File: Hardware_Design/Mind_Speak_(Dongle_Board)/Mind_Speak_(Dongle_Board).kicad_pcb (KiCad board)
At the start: 2 copper layers, 38 x 24.5 mm, 27 parts, among them J1 USB_A, J3 Conn_01x05_Pin, J4 Conn_01x05_Pin, SW3 SW_MEC_5E, U1 FT231XQ, U2 NINA-B30x

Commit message: Dongle Layout Finished
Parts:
- added C14: 0.1uF, PCM_SparkFun-Capacitor:C_0402_1005Metric, F.Cu at (120.3, 72.6)
- added G***: LOGO, Graphics:Mo3_Tech_Logo, F.Cu at (104.8, 57.7)
- moved C11 21.4 mm to (124.0, 72.1), turned to 180 degrees
- moved R5 13.9 mm to (108.9, 70.3)
- moved D4 12.5 mm to (108.3, 71.7), turned to 180 degrees
- moved C13 11.6 mm to (103.0, 69.3), turned to 180 degrees
- moved R6 11.6 mm to (109.9, 68.9), turned to 180 degrees
- moved SW3 11.2 mm to (112.1, 60.5), turned to -90 degrees
- moved R7 9.03 mm to (111.3, 64.0)
- moved R4 6.82 mm to (106.8, 61.3)
- moved G* 5.66 mm to (104.6, 63.0)
- moved J4 2.86 mm to (117.2, 56.2)
- moved D5 1.79 mm to (108.8, 63.5), turned to -90 degrees
- moved D3 1.53 mm to (101.7, 71.0)
- moved L1 1.47 mm to (99.2, 60.6)
- moved D2 1.34 mm to (101.3, 63.2)
- moved C2 1.28 mm to (101.0, 64.3)
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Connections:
- J3 pad 2: SWD_CLK -> SWD_IO
- J3 pad 3: SWD_IO -> SWD_CLK
- U2 pad 18: unconnected-(U2-GPIO_18-Pad18) -> Net-(J4-Pin_5)
- U2 pad 20: unconnected-(U2-GPIO_20-Pad20) -> Net-(J4-Pin_4)
- U2 pad 21: unconnected-(U2-GPIO_21-Pad21) -> Net-(J4-Pin_3)
- U2 pad 22: unconnected-(U2-GPIO_22-Pad22) -> Net-(J4-Pin_2)
- U2 pad 23: unconnected-(U2-GPIO_23-Pad23) -> Net-(J4-Pin_1)
- U2 pad 35: Net-(J4-Pin_5) -> unconnected-(U2-GPIO_35-Pad35)
- U2 pad 36: Net-(J4-Pin_4) -> unconnected-(U2-GPIO_36-Pad36)
- U2 pad 37: Net-(J4-Pin_3) -> unconnected-(U2-GPIO_37-Pad37)
- U2 pad 38: Net-(J4-Pin_2) -> unconnected-(U2-GPIO_38-Pad38)
- U2 pad 39: Net-(J4-Pin_1) -> unconnected-(U2-GPIO_39-Pad39)
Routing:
- net NINA_RST: track 0.00 -> 42.3 mm, vias 0 -> 4
- net +3V3: track 0.00 -> 28.2 mm, vias 0 -> 2
- net GND: track 0.00 -> 20.4 mm, vias 0 -> 17
- net NINA_PWR: track 0.00 -> 18.5 mm
- net SWD_IO: track 0.00 -> 14.6 mm, vias 0 -> 2
- net Net-(J1-GND): track 0.00 -> 13.7 mm
- net FTDI_RX: track 0.00 -> 12.5 mm
- net FTDI_TX: track 0.00 -> 11.8 mm, vias 0 -> 2
- net SWD_CLK: track 0.00 -> 9.29 mm, vias 0 -> 2
- net VBUS: track 0.00 -> 8.92 mm
- net Net-(J1-D+): track 0.00 -> 8.40 mm
- net Net-(U1-CBUS2): track 0.00 -> 7.97 mm
- net Net-(J1-D-): track 0.00 -> 7.83 mm
- net Net-(J4-Pin_5): track 0.00 -> 7.36 mm
- net Net-(J4-Pin_4): track 0.00 -> 7.14 mm
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- added copper zone on B.Cu, net GND
- added copper zone on F.Cu, net GND
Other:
- board text added: "BLE_PWR"
- board text added: "GND"
- board text added: "GPIO_18"
- board text added: "GPIO_20"
- board text added: "GPIO_21"
- board text added: "GPIO_22"
- board text added: "GPIO_23"
- board text added: "RESET"
- board text added: "SWD"
- board text added: "SWD_CLK"
- board text added: "SWD_IO"
- board text added: "SWD_RST"
- board text added: "SWD_VCC"
- board text added: "USB"

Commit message: Edit In Layout Of Main Board
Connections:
- J1 pad SH: unconnected-(J1-Shield-PadSH)_1 -> GND
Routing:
- net GND: track 20.4 -> 16.0 mm, vias 17 -> 26
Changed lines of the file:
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@@
 			(unit
 				(name "A")
-				(pins "1" "2" "3")
+				(pins "4" "1" "2" "3")
 			)
 		)
@@
 			(solder_mask_margin 0.102)
 		)
-		(pad "SH1" smd rect
+		(pad "4" smd rect
 			(at -3.65 -1.1)
 			(size 1 0.8)
 			(layers "F.Cu" "F.Mask" "F.Paste")
+			(net "GND")
+			(pinfunction "SHIELD_4")
+			(pintype "passive")
 			(solder_mask_margin 0.102)
 		)
-		(pad "SH2" smd rect
-			(at 3.65 -1.1)
+		(pad "4" smd rect
+			(at -3.65 1.1)
 			(size 1 0.8)
 			(layers "F.Cu" "F.Mask" "F.Paste")
+			(net "GND")
+			(pinfunction "SHIELD_4")
+			(pintype "passive")
 			(solder_mask_margin 0.102)
 		)
-		(pad "SH3" smd rect
-			(at -3.65 1.1)
+		(pad "4" smd rect
+			(at 3.65 -1.1)
 			(size 1 0.8)
 			(layers "F.Cu" "F.Mask" "F.Paste")
+			(net "GND")
+			(pinfunction "SHIELD_4")
+			(pintype "passive")
 			(solder_mask_margin 0.102)
 		)
-		(pad "SH4" smd rect
+		(pad "4" smd rect
 			(at 3.65 1.1)
 			(size 1 0.8)
 			(layers "F.Cu" "F.Mask" "F.Paste")
+			(net "GND")
+			(pinfunction "SHIELD_4")
+			(pintype "passive")
 			(solder_mask_margin 0.102)
 		)
@@
 			(layers "*.Cu" "*.Mask")
 			(remove_unused_layers no)
-			(net "unconnected-(J1-Shield-PadSH)")
+			(net "GND")
 			(pinfunction "Shield_SH")
-			(pintype "passive+no_connect")
+			(pintype "passive")
 			(solder_mask_margin 0.0762)
 		)
@@
 			(layers "*.Cu" "*.Mask")
 			(remove_unused_layers no)
-			(net "unconnected-(J1-Shield-PadSH)_1")
+			(net "GND")
 			(pinfunction "Shield_SH")
-			(pintype "passive+no_connect")
+			(pintype "passive")
 			(solder_mask_margin 0.0762)
 		)
@@
 	)
 	(segment
-		(start 106.36 76.26)
-		(end 106.12 76.5)
-		(width 0.2)
-		(layer "F.Cu")
-		(net "GND")
-	)
-	(segment
-		(start 105.55 66.4)
-		(end 105.55 64.4625)
-		(width 0.2)
-		(layer "F.Cu")
-		(net "GND")
-	)
-	(segment
 		(start 124.1 67)
 		(end 125.2 67)
@@
 	)
 	(segment
-		(start 105.55 66.4)
-		(end 105.55 68.3375)
-		(width 0.2)
-		(layer "F.Cu")
-		(net "GND")
-	)
-	(segment
 		(start 126.275 60.275)
 		(end 126.275 61.65)
@@
 	)
 	(segment
+		(start 106.36 76.09)
+		(end 106.36 74.97)
+		(width 0.2)
+		(layer "F.Cu")
+		(net "GND")
+	)
+	(segment
 		(start 105.55 64.4625)
 		(end 105.55 63.1)
@@
 		(net "GND")
 	)
-	(segment
-		(start 106.36 74.97)
-		(end 106.36 76.26)
-		(width 0.2)
-		(layer "F.Cu")
+	(via
+		(at 119.1 67.6)
+		(size 0.8)
+		(drill 0.3)
+		(layers "F.Cu" "B.Cu")
+		(free yes)
 		(net "GND")
 	)
 	(via
-		(at 119.1 67.6)
+		(at 104.72 65.6)
+		(size 0.8)
+		(drill 0.3)
+		(layers "F.Cu" "B.Cu")
+		(free yes)
+		(net "GND")
+	)
+	(via
+		(at 106.35 67.18)
 		(size 0.8)
 		(drill 0.3)
@@
 	)
 	(via
+		(at 115.2 76.77)
+		(size 0.8)
+		(drill 0.3)
+		(layers "F.Cu" "B.Cu")
+		(free yes)
+		(net "GND")
+	)
+	(via
+		(at 96.3 58.82)
+		(size 0.8)
+		(drill 0.3)
+		(layers "F.Cu" "B.Cu")
+		(free yes)
+		(net "GND")
+	)
+	(via
+		(at 93.91 73.94)
+		(size 0.8)
+		(drill 0.3)
+		(layers "F.Cu" "B.Cu")
+		(free yes)
+		(net "GND")
+	)
+	(via
 		(at 113.05 60.5)
 		(size 0.8)
@@
 	)
 	(via
+		(at 96.3 73.94)
+		(size 0.8)
+		(drill 0.3)
+		(layers "F.Cu" "B.Cu")
+		(free yes)
+		(net "GND")
+	)
+	(via
+		(at 106.35 65.6)
+		(size 0.8)
+		(drill 0.3)
+		(layers "F.Cu" "B.Cu")
+		(free yes)
+		(net "GND")
+	)
+	(via
+		(at 104.72 67.18)
+		(size 0.8)
+		(drill 0.3)
+		(layers "F.Cu" "B.Cu")
+		(free yes)
+		(net "GND")
+	)
+	(via
 		(at 121.59 71.78)
 		(size 0.8)
@@
 	)
 	(via
-		(at 106.12 76.5)
+		(at 106.36 76.09)
+		(size 0.8)
+		(drill 0.3)
+		(layers "F.Cu" "B.Cu")
+		(free yes)
+		(net "GND")
+	)
+	(via
+		(at 101.89 63.28)
 		(size 0.8)
 		(drill 0.3)
@@
 	)
 	(via
-		(at 101.24 60.23)
+		(at 93.91 58.84)
 		(size 0.8)
 		(drill 0.3)

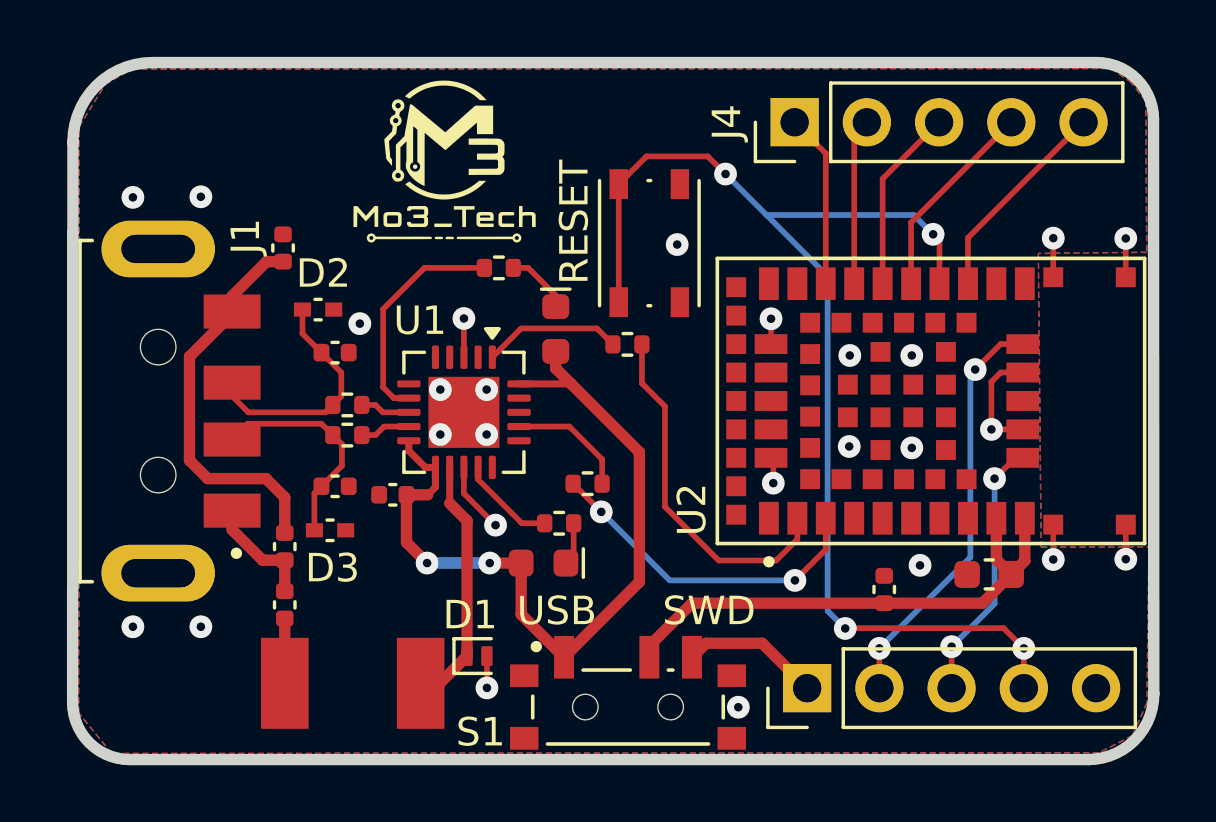
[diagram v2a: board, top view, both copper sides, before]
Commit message: Edit in Dongle/Main Boards
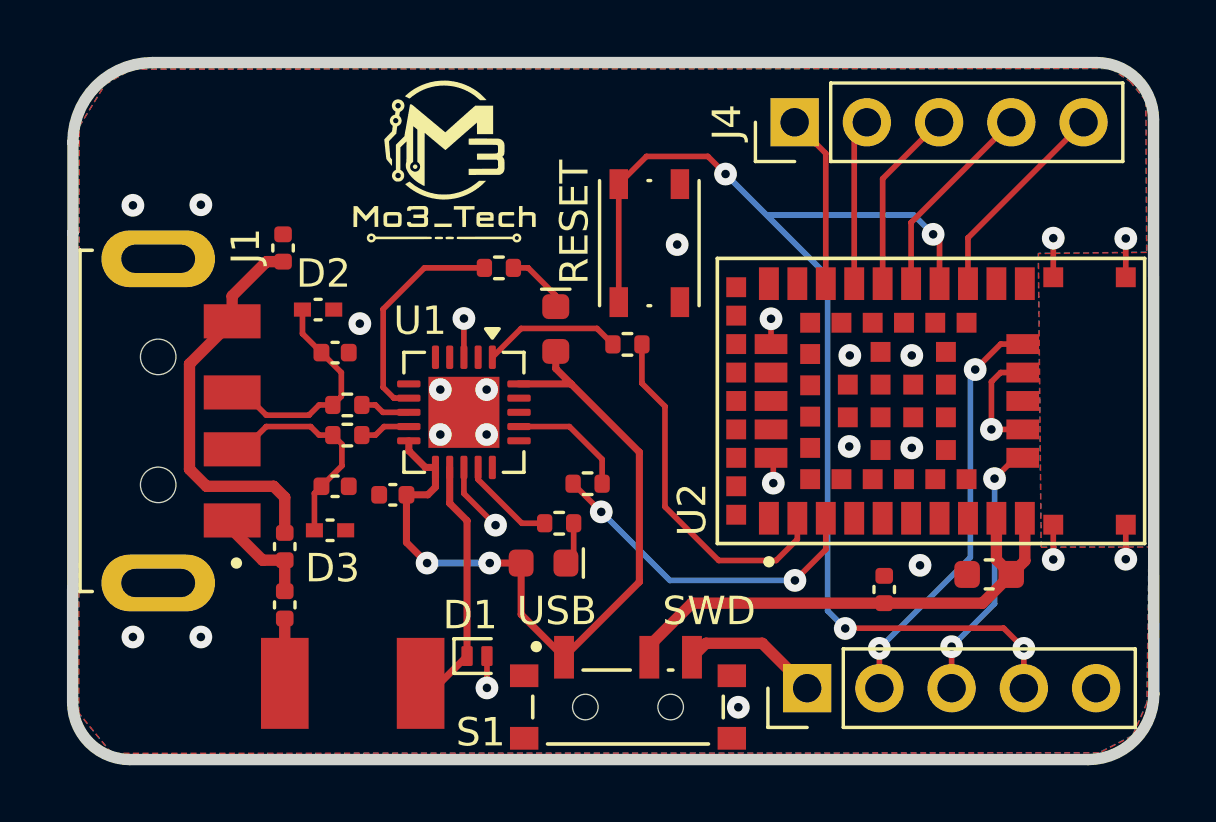
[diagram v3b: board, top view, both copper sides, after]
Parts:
- moved J1 0.34 mm to (94.8, 66.7)
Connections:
- net Net-(J1-D+) renamed /D+
- net Net-(J1-D-) renamed /D-
